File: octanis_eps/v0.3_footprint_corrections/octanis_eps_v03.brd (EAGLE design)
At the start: 61.9 x 49.5 mm, 100 parts, among them IC1 OPA2333DGK, IC5 OPA2333DGK, IC7 OPA2333DGK, IC9 OPA2333DGK, Q1 FC-12M, Q2 N-HEXFET-2D_SOT232-, Q3 N-HEXFET-2D_SOT232-, Q4 N-HEXFET-2D_SOT232-

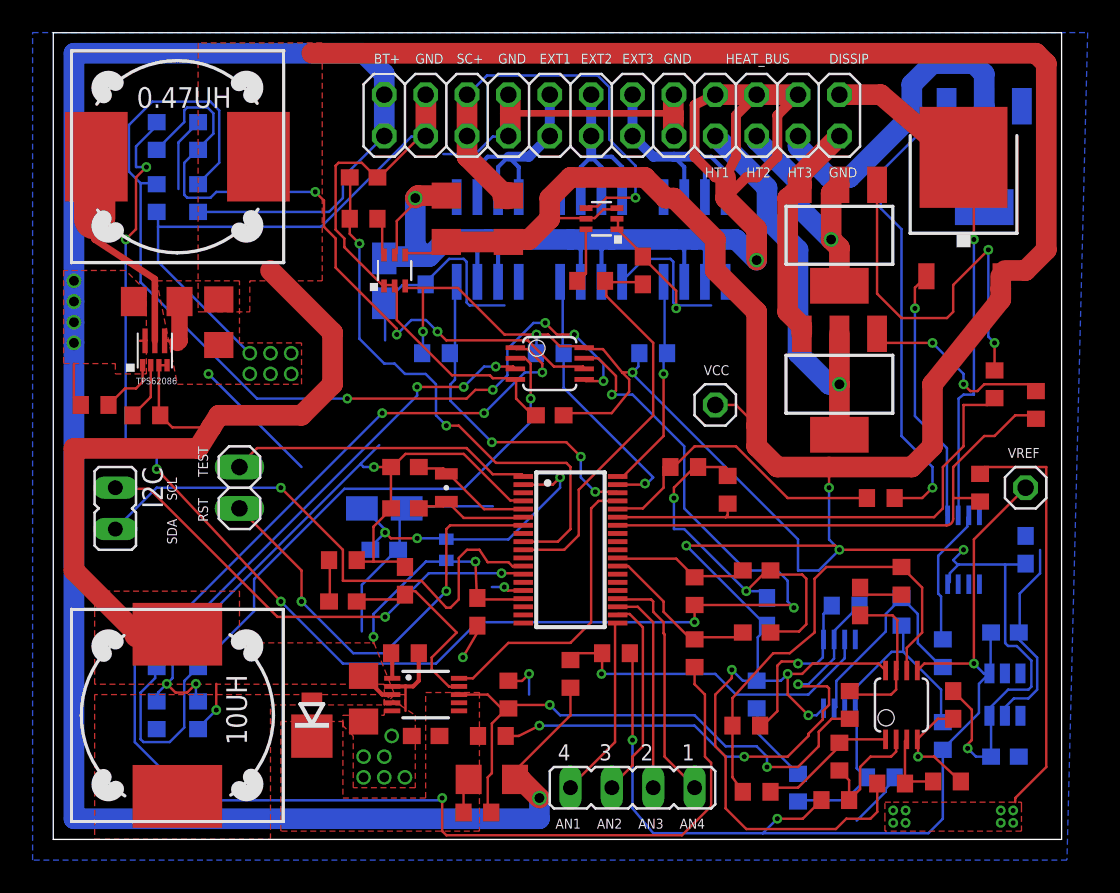
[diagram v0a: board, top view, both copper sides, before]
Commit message: corrected footprints for MSP & Step down, 50mOhms still to be changed (4points probe)
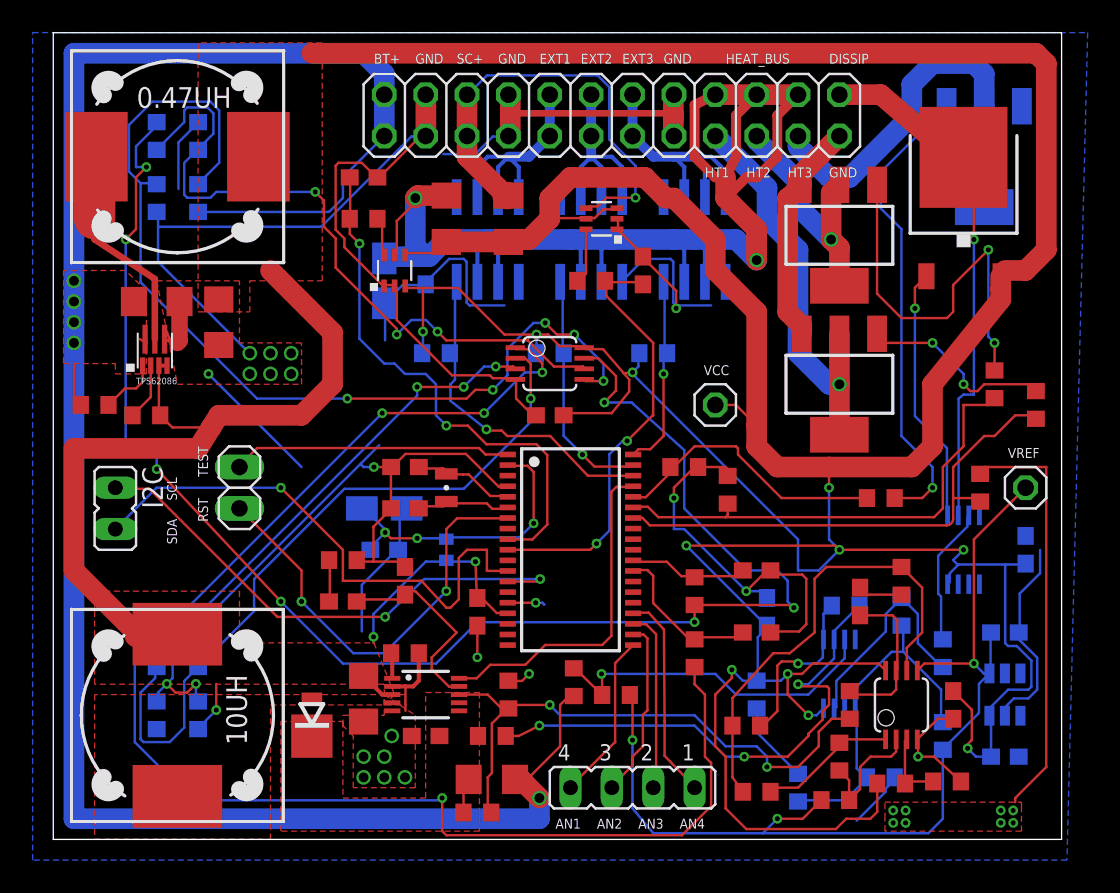
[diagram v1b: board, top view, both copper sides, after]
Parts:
- U$6: device Octanis1_EPS:TSSOP38 -> Octanis1_EPS:TSSOP38_MSPGXX44_SERIES
- moved R40 2.57 mm to (34.5, 39.3)
- moved R39 0.55 mm to (32.0, 40.1)
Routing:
- net GND: track 282.0 -> 275.1 mm
- net I2C_SCL: track 29.4 -> 32.3 mm
- net VREF: track 63.8 -> 61.2 mm
- net EN_CHG: track 18.3 -> 20.8 mm
- net EN_EXT2: track 16.8 -> 14.7 mm
- net I_SC: track 24.8 -> 26.9 mm, vias 0 -> 2
- net A_EXT4: track 14.7 -> 12.8 mm
- net I_EXT_PW: track 34.5 -> 32.8 mm
- net A_EXT3: track 12.7 -> 11.2 mm
- net EN_HEAT3: track 18.9 -> 17.4 mm
- net EN_EXT3: track 13.7 -> 12.2 mm
- net TEST/SBWTCK: track 18.7 -> 17.2 mm
- net A_EXT2: track 12.6 -> 11.0 mm
- net N$48: track 7.56 -> 6.29 mm
- net N$50: track 7.08 -> 5.92 mm
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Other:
- board text added: "Octanis_EPS v0.3"
- board text removed: "Octanis_EPS v0.2"
